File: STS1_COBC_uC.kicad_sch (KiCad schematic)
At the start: 44 parts, among them J16 SWD, U18 STWD100PYW83F, U19 STM32F411RET6TR, U28 MCP130T-300I_TT, U29 74LVC1G08GV,125, U31 74LVC1G08GV,125, U32 74LVC1G32GV,125, Y1 12M

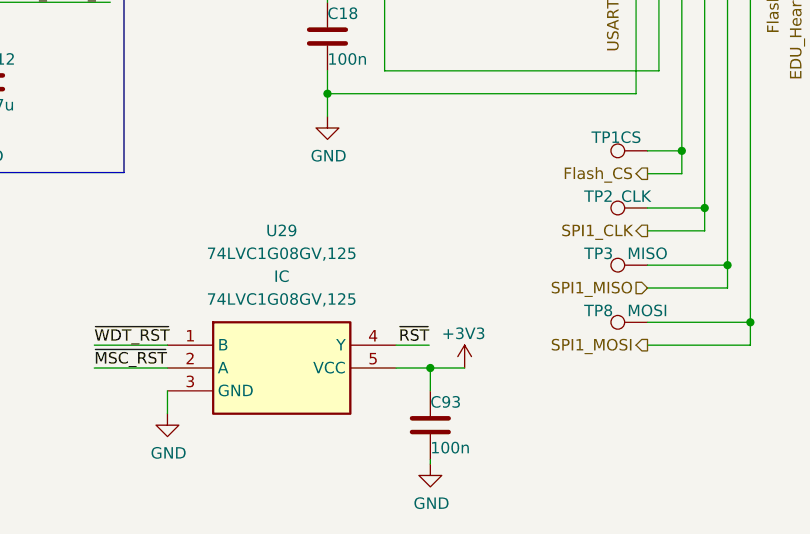
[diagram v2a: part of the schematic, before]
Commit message: Decouple U29 from the ~RST comming from the JTAG connector
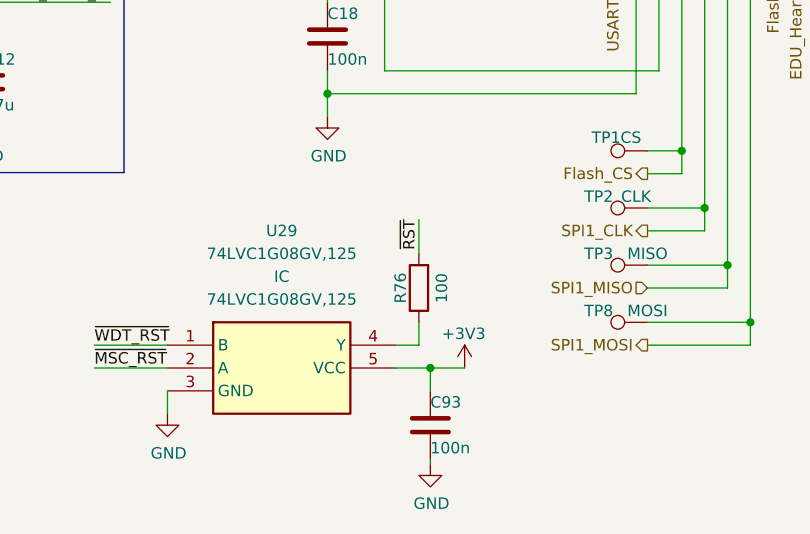
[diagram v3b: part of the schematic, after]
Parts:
- added R76: 100, Resistor_SMD:R_0603_1608Metric, symbol Device:R
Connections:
- net UCI_COBC_NOT_RST: now also R76.2; no longer U29.4 (Y)
- new net: R76.1, U29.4 (Y)
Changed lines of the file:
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@@
+    (stroke (width 0) (type default) (color 0 0 0 0))
+  )
+  (wire (pts (xy 107.95 177.8) (xy 107.95 175.26))
     (stroke (width 0) (type default) (color 0 0 0 0))
   )
@@
     (stroke (width 0) (type default) (color 0 0 0 0))
   )
+  (wire (pts (xy 105.41 177.8) (xy 107.95 177.8))
+    (stroke (width 0) (type default) (color 0 0 0 0))
+  )
   (polyline (pts (xy 15.24 116.713) (xy 15.24 158.623))
     (stroke (width 0) (type default) (color 0 0 0 0))
@@
     (stroke (width 0) (type default) (color 0 0 0 0))
   )
-  (wire (pts (xy 105.41 177.8) (xy 109.093 177.8))
-    (stroke (width 0) (type default) (color 0 0 0 0))
-  )
   (wire (pts (xy 40.64 76.2) (xy 40.64 78.74))
     (stroke (width 0) (type default) (color 0 0 0 0))
@@
   )
   (polyline (pts (xy 222.25 130.81) (xy 222.25 165.1))
+    (stroke (width 0) (type default) (color 0 0 0 0))
+  )
+  (wire (pts (xy 107.95 163.83) (xy 107.95 167.64))
     (stroke (width 0) (type default) (color 0 0 0 0))
   )
@@
     (effects (font (size 1.27 1.27)) (justify left bottom))
   )
-  (label "~{RST}" (at 109.093 177.8 180)
+  (label "~{RST}" (at 107.95 163.83 270)
     (effects (font (size 1.27 1.27)) (justify right bottom))
   )
@@
     (pin "1")
   )
+  (symbol (lib_id "Device:R") (at 107.95 171.45 180) (unit 1)
+    (in_bom yes) (on_board yes)
+    (property "Reference" "R76" (id 0) (at 105.918 171.45 90))
+    (property "Value" "100" (id 1) (at 110.49 171.45 90))
+    (property "Footprint" "Resistor_SMD:R_0603_1608Metric" (id 2) (at 109.728 171.45 90)
+      (effects (font (size 1.27 1.27)) hide)
+    )
+    (property "Datasheet" "~" (id 3) (at 107.95 171.45 0)
+      (effects (font (size 1.27 1.27)) hide)
+    )
+    (property "JLCPCB Part #" "C2074896" (id 4) (at 107.95 171.45 0)
+      (effects (font (size 1.27 1.27)) hide)
+    )
+    (property "Manufacturer_Part_Number" "CRS0603AFX-1000ELF" (id 5) (at 107.95 171.45 0)
+      (effects (font (size 1.27 1.27)) hide)
+    )
+    (pin "1")
+    (pin "2")
+  )
   (symbol (lib_id "Device:C") (at 273.05 154.94 180) (unit 1)

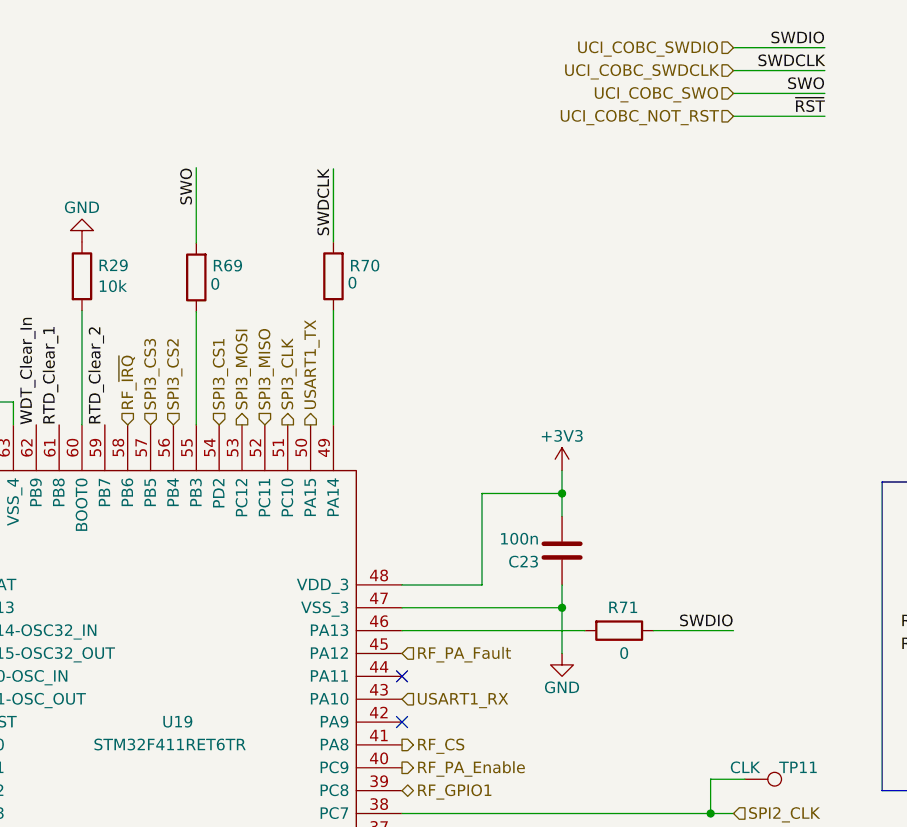
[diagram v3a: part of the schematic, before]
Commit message: Do not populate R69, R70 and R71 on the flight model CSBI-JTAG interface won't be used
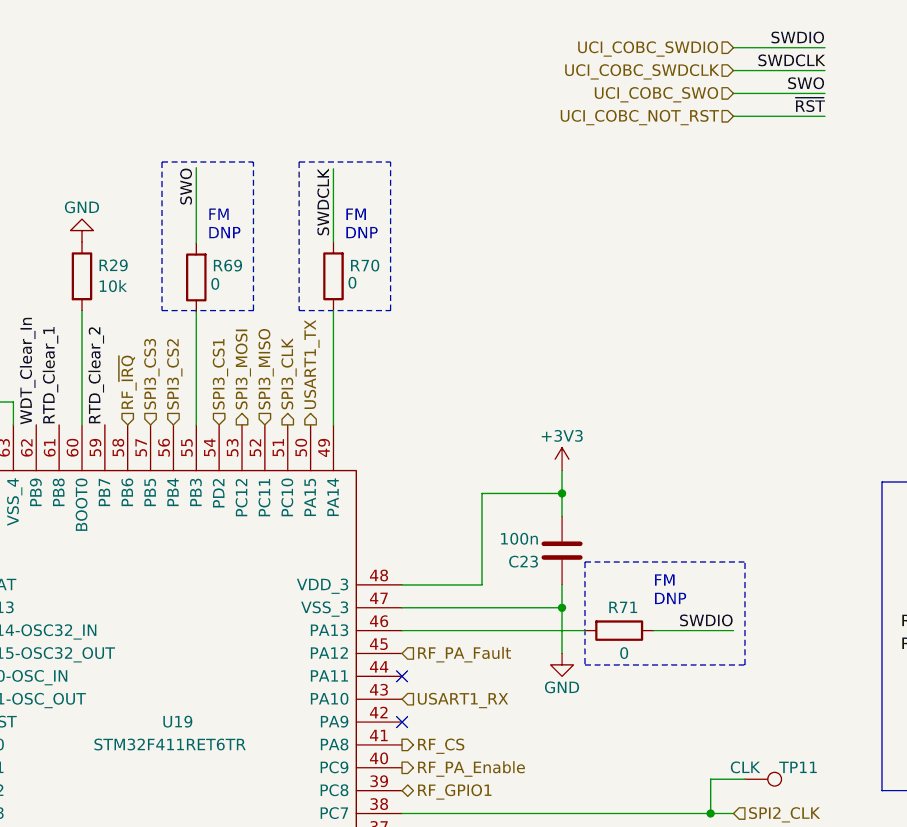
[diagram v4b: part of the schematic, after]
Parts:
- R69: now left out of the parts list
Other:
- note added: "FM DNP"
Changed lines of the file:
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@@
     (stroke (width 0) (type default) (color 0 0 0 0))
+  )
+  (polyline (pts (xy 148.59 30.48) (xy 148.59 46.99))
+    (stroke (width 0) (type dot) (color 0 0 0 0))
   )
   (wire (pts (xy 203.2 82.55) (xy 212.09 82.55))
@@
     (stroke (width 0) (type default) (color 0 0 0 0))
   )
+  (polyline (pts (xy 163.83 30.48) (xy 163.83 46.99))
+    (stroke (width 0) (type dot) (color 0 0 0 0))
+  )
   (wire (pts (xy 134.62 133.35) (xy 134.62 147.32))
     (stroke (width 0) (type default) (color 0 0 0 0))
@@
     (stroke (width 0) (type default) (color 0 0 0 0))
   )
+  (polyline (pts (xy 195.58 86.36) (xy 213.36 86.36))
+    (stroke (width 0) (type dot) (color 0 0 0 0))
+  )
   (wire (pts (xy 107.95 177.8) (xy 107.95 175.26))
     (stroke (width 0) (type default) (color 0 0 0 0))
@@
     (stroke (width 0) (type default) (color 0 0 0 0))
   )
+  (polyline (pts (xy 173.99 46.99) (xy 173.99 30.48))
+    (stroke (width 0) (type dot) (color 0 0 0 0))
+  )
   (wire (pts (xy 167.64 31.242) (xy 167.64 39.37))
     (stroke (width 0) (type default) (color 0 0 0 0))
@@
     (stroke (width 0) (type default) (color 0 0 0 0))
   )
+  (polyline (pts (xy 213.36 86.36) (xy 213.36 74.93))
+    (stroke (width 0) (type dot) (color 0 0 0 0))
+  )
   (wire (pts (xy 133.35 162.56) (xy 139.7 162.56))
     (stroke (width 0) (type default) (color 0 0 0 0))
@@
     (stroke (width 0) (type default) (color 0 0 0 0))
   )
+  (polyline (pts (xy 163.83 30.48) (xy 173.99 30.48))
+    (stroke (width 0) (type dot) (color 0 0 0 0))
+  )
   (wire (pts (xy 76.2 100.33) (xy 81.28 100.33))
     (stroke (width 0) (type default) (color 0 0 0 0))
@@
     (stroke (width 0) (type default) (color 0 0 0 0))
   )
+  (polyline (pts (xy 163.83 46.99) (xy 173.99 46.99))
+    (stroke (width 0) (type dot) (color 0 0 0 0))
+  )
   (wire (pts (xy 137.16 156.21) (xy 137.16 158.75))
     (stroke (width 0) (type default) (color 0 0 0 0))
@@
     (stroke (width 0) (type default) (color 0 0 0 0))
   )
+  (polyline (pts (xy 148.59 30.48) (xy 158.75 30.48))
+    (stroke (width 0) (type dot) (color 0 0 0 0))
+  )
   (wire (pts (xy 46.99 81.28) (xy 46.99 83.82))
     (stroke (width 0) (type default) (color 0 0 0 0))
@@
     (stroke (width 0) (type default) (color 0 0 0 0))
   )
+  (polyline (pts (xy 195.58 74.93) (xy 213.36 74.93))
+    (stroke (width 0) (type dot) (color 0 0 0 0))
+  )
   (polyline (pts (xy 228.6 66.04) (xy 228.6 100.33))
     (stroke (width 0) (type default) (color 0 0 0 0))
@@
     (stroke (width 0) (type default) (color 0 0 0 0))
   )
+  (polyline (pts (xy 158.75 46.99) (xy 158.75 30.48))
+    (stroke (width 0) (type dot) (color 0 0 0 0))
+  )
   (wire (pts (xy 133.35 177.8) (xy 144.78 177.8))
     (stroke (width 0) (type default) (color 0 0 0 0))
@@
   (wire (pts (xy 104.14 147.32) (xy 104.14 137.16))
     (stroke (width 0) (type default) (color 0 0 0 0))
+  )
+  (polyline (pts (xy 148.59 46.99) (xy 158.75 46.99))
+    (stroke (width 0) (type dot) (color 0 0 0 0))
+  )
+  (polyline (pts (xy 195.58 74.93) (xy 195.58 86.36))
+    (stroke (width 0) (type dot) (color 0 0 0 0))
   )
   (wire (pts (xy 47.498 184.531) (xy 47.498 186.055))
@@
     (effects (font (size 1.27 1.27)) (justify left bottom))
   )
+  (text "FM\nDNP\n" (at 168.91 39.37 0)
+    (effects (font (size 1.27 1.27)) (justify left bottom))
+  )
   (text "Add some redundancy when disabling the\nlatch-up protection of the RF part:\nof two STM pins, at least one should be high"
     (at 232.41 99.06 0)
@@
   )
   (text "Watchdog Timer" (at 34.163 157.861 0)
+    (effects (font (size 1.27 1.27)) (justify left bottom))
+  )
+  (text "FM\nDNP\n" (at 153.67 39.37 0)
+    (effects (font (size 1.27 1.27)) (justify left bottom))
+  )
+  (text "FM\nDNP\n" (at 203.2 80.01 0)
     (effects (font (size 1.27 1.27)) (justify left bottom))
   )
@@
   )
   (symbol (lib_id "Device:R") (at 152.4 43.307 180) (unit 1)
-    (in_bom yes) (on_board yes)
+    (in_bom no) (on_board yes)
     (property "Reference" "R69" (id 0) (at 157.607 42.037 0)
       (effects (font (size 1.27 1.27)) (justify left))

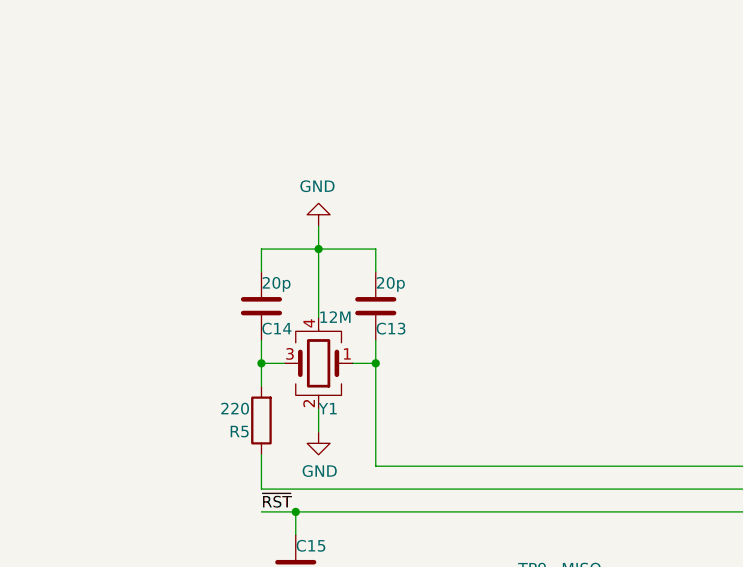
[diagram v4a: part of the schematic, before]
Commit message: Update the 12 MHz crystal oscillator value and change the related capacitors: C13, C14 20 pF -> 13 pF
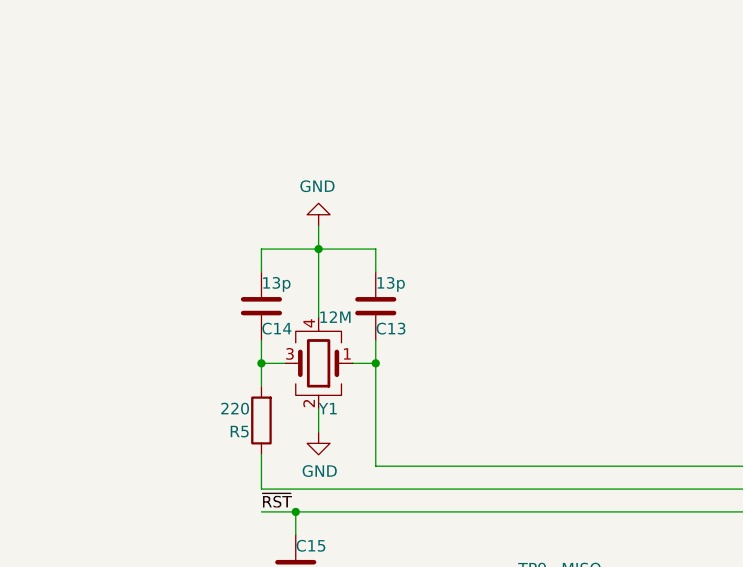
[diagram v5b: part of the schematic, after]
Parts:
- C13, C14: value 20p -> 13p; JLCPCB Part # C1648 -> (none); Manufacturer_Part_Number CL10C200JB8NNNC -> (none)
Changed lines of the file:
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@@
       (effects (font (size 1.27 1.27)) (justify left))
     )
-    (property "Value" "20p" (id 1) (at 53.34 67.31 0)
+    (property "Value" "13p" (id 1) (at 53.34 67.31 0)
       (effects (font (size 1.27 1.27)) (justify left))
     )
@@
       (effects (font (size 1.27 1.27)) hide)
     )
-    (property "JLCPCB Part #" "C1648" (id 4) (at 53.34 69.85 0)
+    (property "JLCPCB Part #" "" (id 4) (at 53.34 69.85 0)
       (effects (font (size 1.27 1.27)) hide)
     )
-    (property "Manufacturer_Part_Number" "CL10C200JB8NNNC " (id 5) (at 53.34 69.85 0)
+    (property "Manufacturer_Part_Number" "" (id 5) (at 53.34 69.85 0)
       (effects (font (size 1.27 1.27)) hide)
     )
@@
       (effects (font (size 1.27 1.27)) (justify left))
     )
-    (property "Value" "20p" (id 1) (at 40.64 67.31 0)
+    (property "Value" "13p" (id 1) (at 40.64 67.31 0)
       (effects (font (size 1.27 1.27)) (justify left))
     )
@@
       (effects (font (size 1.27 1.27)) hide)
     )
-    (property "JLCPCB Part #" "C1648" (id 4) (at 40.64 69.85 0)
+    (property "JLCPCB Part #" "" (id 4) (at 40.64 69.85 0)
       (effects (font (size 1.27 1.27)) hide)
     )
-    (property "Manufacturer_Part_Number" "CL10C200JB8NNNC " (id 5) (at 40.64 69.85 0)
+    (property "Manufacturer_Part_Number" "" (id 5) (at 40.64 69.85 0)
       (effects (font (size 1.27 1.27)) hide)
     )

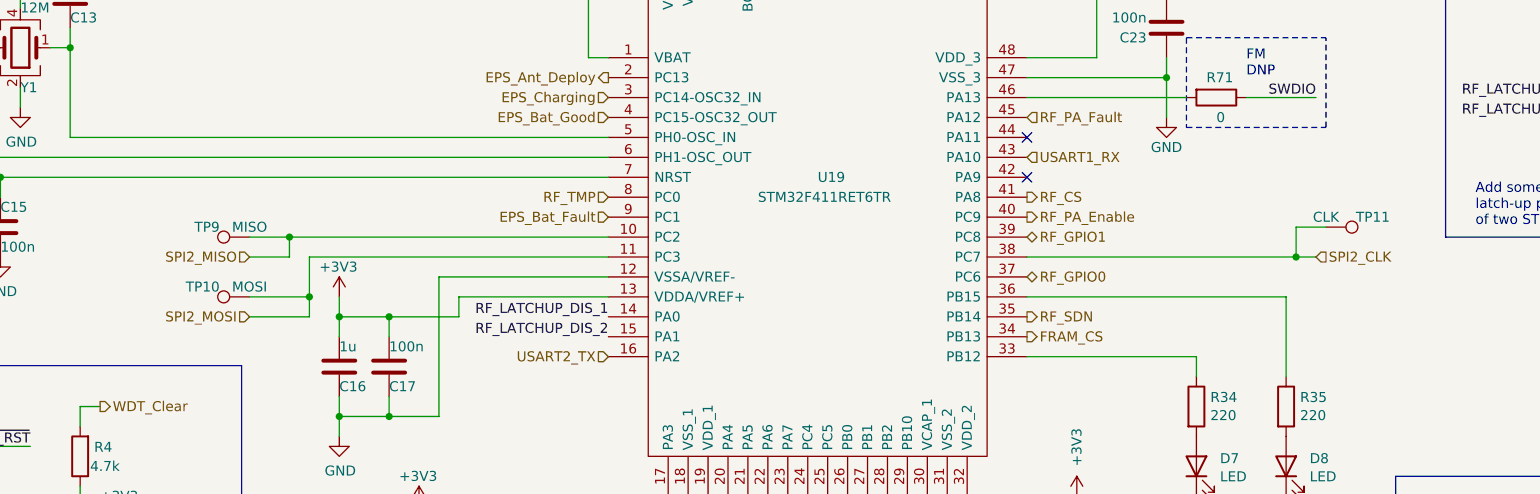
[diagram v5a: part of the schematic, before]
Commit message: Fix power domain crossing issue between RF and STM units
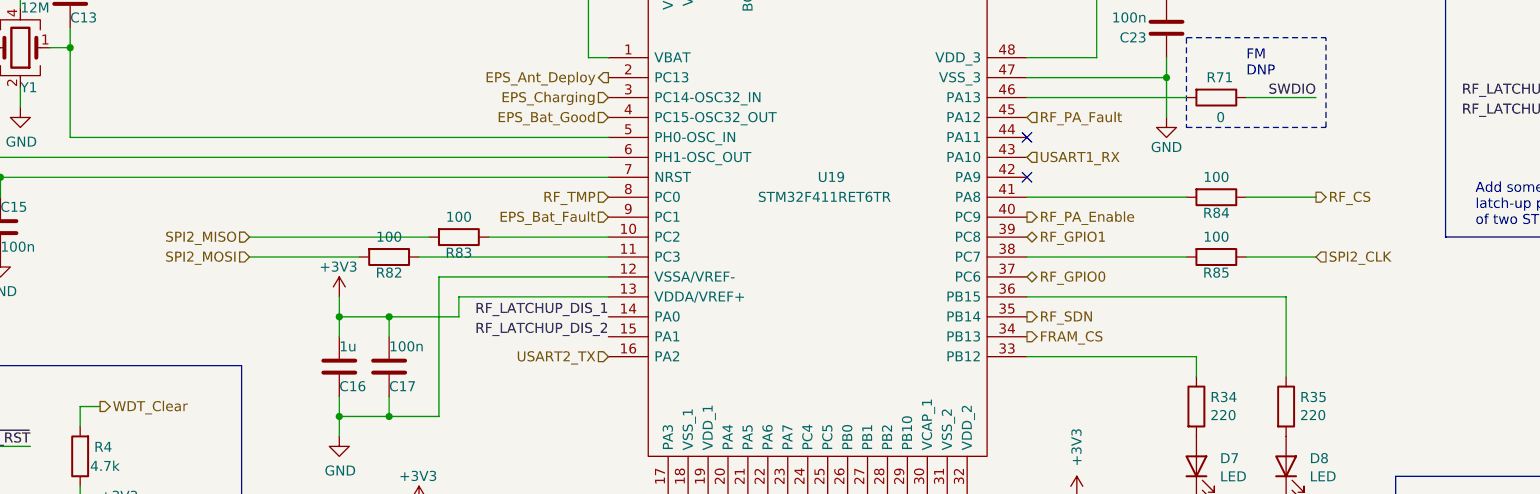
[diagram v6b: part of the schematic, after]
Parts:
- removed TP10: MOSI, STS1library:STS1_Testpoint, symbol Connector:TestPoint
- removed TP11: CLK, STS1library:STS1_Testpoint, symbol Connector:TestPoint
- removed TP9: MISO, STS1library:STS1_Testpoint, symbol Connector:TestPoint
- added R82, R83, R84, R85: 100, Resistor_SMD:R_0603_1608Metric, symbol Device:R
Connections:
- net RF_CS: now also R84.1; no longer U19.41 (PA8)
- net SPI2_CLK: now also R85.1; no longer U19.38 (PC7)
- net SPI2_MISO: now also R83.2; no longer U19.10 (PC2)
- net SPI2_MOSI: now also R82.2; no longer U19.11 (PC3)
- new net: R83.1, U19.10 (PC2)
- new net: R82.1, U19.11 (PC3)
- new net: R85.2, U19.38 (PC7)
- new net: R84.2, U19.41 (PA8)
